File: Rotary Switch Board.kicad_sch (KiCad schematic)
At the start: 9 parts, among them SW1 1P8T_ROTARY_SWITCH

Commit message: included larger resistor
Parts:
- R1, R2, R3, R4, R5, R6, R7: footprint Resistor_THT:R_Axial_DIN0204_L3.6mm_D1.6mm_P5.08mm_Horizontal -> Resistor_THT:R_Axial_DIN0204_L3.6mm_D1.6mm_P7.62mm_Horizontal

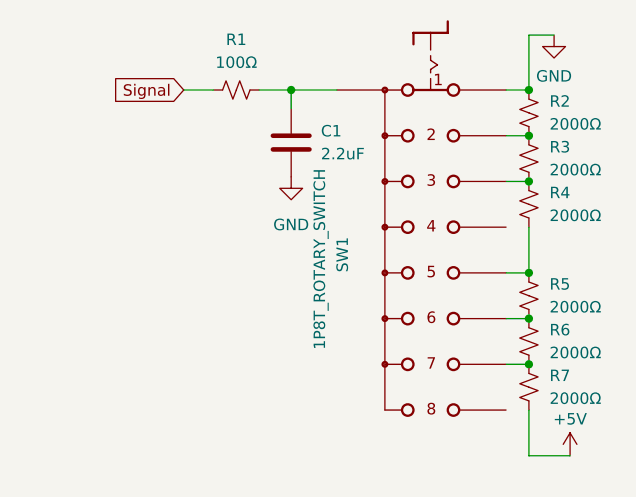
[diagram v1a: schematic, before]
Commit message: allowed for connection of all 8 pins, now you can just skip the ones you dont need
now you can just skip the ones you dont need
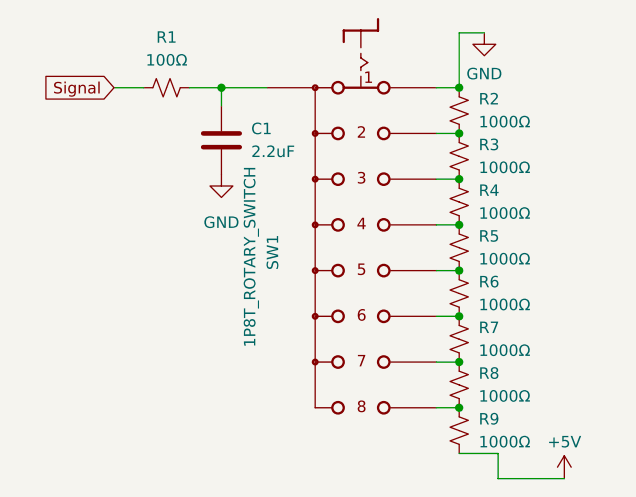
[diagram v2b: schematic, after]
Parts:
- added R5, R9: 1000Ω, Resistor_THT:R_Axial_DIN0204_L3.6mm_D1.6mm_P7.62mm_Horizontal, symbol Device:R_Small_US
- R2, R3, R4: value 2000Ω -> 1000Ω
- R6: renamed from R5; value 2000Ω -> 1000Ω
- R7: renamed from R6; value 2000Ω -> 1000Ω
- R8: renamed from R7; value 2000Ω -> 1000Ω
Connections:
- net +5V: now also R9.2; no longer R8.2
- net at R6.1, SW1.5: now also R5.2; no longer R4.2
- net at SW1.4: now also R4.2, R5.1
- net at SW1.8: now also R8.2, R9.1
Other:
- moved on the sheet: C1, R1, R2, R3, R4, R6, R7, R8, SW1

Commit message: redid traces
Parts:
- R1, R2, R3, R4, R5, R6, R7, R8, R9: footprint Resistor_THT:R_Axial_DIN0204_L3.6mm_D1.6mm_P7.62mm_Horizontal -> Resistor_THT:R_Axial_DIN0204_L3.6mm_D1.6mm_P5.08mm_Horizontal
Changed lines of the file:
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@@
       (effects (font (size 1.27 1.27)) (justify left))
     )
-    (property "Footprint" "Resistor_THT:R_Axial_DIN0204_L3.6mm_D1.6mm_P7.62mm_Horizontal" (at 139.954 82.042 0)
+    (property "Footprint" "Resistor_THT:R_Axial_DIN0204_L3.6mm_D1.6mm_P5.08mm_Horizontal" (at 139.954 82.042 0)
       (effects (font (size 1.27 1.27)) hide)
     )
@@
       (effects (font (size 1.27 1.27)) (justify left))
     )
-    (property "Footprint" "Resistor_THT:R_Axial_DIN0204_L3.6mm_D1.6mm_P7.62mm_Horizontal" (at 139.954 87.122 0)
+    (property "Footprint" "Resistor_THT:R_Axial_DIN0204_L3.6mm_D1.6mm_P5.08mm_Horizontal" (at 139.954 87.122 0)
       (effects (font (size 1.27 1.27)) hide)
     )
@@
       (effects (font (size 1.27 1.27)) (justify left))
     )
-    (property "Footprint" "Resistor_THT:R_Axial_DIN0204_L3.6mm_D1.6mm_P7.62mm_Horizontal" (at 139.954 71.882 0)
+    (property "Footprint" "Resistor_THT:R_Axial_DIN0204_L3.6mm_D1.6mm_P5.08mm_Horizontal" (at 139.954 71.882 0)
       (effects (font (size 1.27 1.27)) hide)
     )
@@
       (effects (font (size 1.27 1.27)) (justify left))
     )
-    (property "Footprint" "Resistor_THT:R_Axial_DIN0204_L3.6mm_D1.6mm_P7.62mm_Horizontal" (at 139.954 76.962 0)
+    (property "Footprint" "Resistor_THT:R_Axial_DIN0204_L3.6mm_D1.6mm_P5.08mm_Horizontal" (at 139.954 76.962 0)
       (effects (font (size 1.27 1.27)) hide)
     )
@@
       (effects (font (size 1.27 1.27)))
     )
-    (property "Footprint" "Resistor_THT:R_Axial_DIN0204_L3.6mm_D1.6mm_P7.62mm_Horizontal" (at 107.442 69.342 0)
+    (property "Footprint" "Resistor_THT:R_Axial_DIN0204_L3.6mm_D1.6mm_P5.08mm_Horizontal" (at 107.442 69.342 0)
       (effects (font (size 1.27 1.27)) hide)
     )
@@
       (effects (font (size 1.27 1.27)) (justify left))
     )
-    (property "Footprint" "Resistor_THT:R_Axial_DIN0204_L3.6mm_D1.6mm_P7.62mm_Horizontal" (at 139.954 107.442 0)
+    (property "Footprint" "Resistor_THT:R_Axial_DIN0204_L3.6mm_D1.6mm_P5.08mm_Horizontal" (at 139.954 107.442 0)
       (effects (font (size 1.27 1.27)) hide)
     )
@@
       (effects (font (size 1.27 1.27)) (justify left))
     )
-    (property "Footprint" "Resistor_THT:R_Axial_DIN0204_L3.6mm_D1.6mm_P7.62mm_Horizontal" (at 139.954 92.202 0)
+    (property "Footprint" "Resistor_THT:R_Axial_DIN0204_L3.6mm_D1.6mm_P5.08mm_Horizontal" (at 139.954 92.202 0)
       (effects (font (size 1.27 1.27)) hide)
     )
@@
       (effects (font (size 1.27 1.27)) (justify left))
     )
-    (property "Footprint" "Resistor_THT:R_Axial_DIN0204_L3.6mm_D1.6mm_P7.62mm_Horizontal" (at 139.954 102.362 0)
+    (property "Footprint" "Resistor_THT:R_Axial_DIN0204_L3.6mm_D1.6mm_P5.08mm_Horizontal" (at 139.954 102.362 0)
       (effects (font (size 1.27 1.27)) hide)
     )
@@
       (effects (font (size 1.27 1.27)) (justify left))
     )
-    (property "Footprint" "Resistor_THT:R_Axial_DIN0204_L3.6mm_D1.6mm_P7.62mm_Horizontal" (at 139.954 97.282 0)
-      (effects (font (size 1.27 1.27)) hide)
-    )
+    (property "Footprint" "Resistor_THT:R_Axial_DIN0204_L3.6mm_D1.6mm_P5.08mm_Horizontal" (at 139.954 97.282 0)
+      (effects (font (size 1.27 1.27)) hide)
+    )
